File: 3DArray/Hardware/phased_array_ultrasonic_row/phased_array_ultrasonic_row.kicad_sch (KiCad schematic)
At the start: 16 parts, among them J1 Conn_02x09_Counter_Clockwise, J2 Conn_02x09_Counter_Clockwise, U1 SN74HC157, U2 SN74HC157

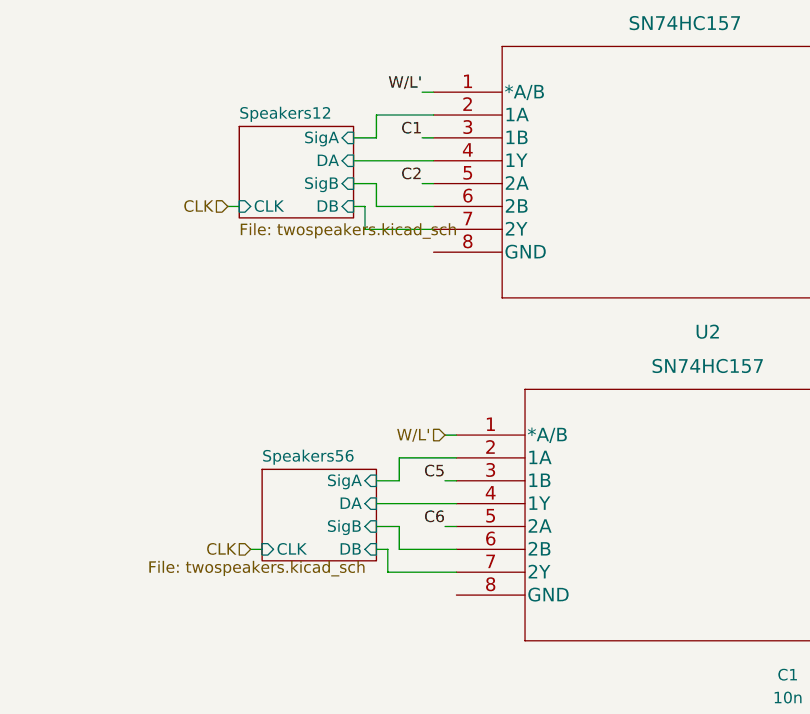
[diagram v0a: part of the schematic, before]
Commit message: Fixed pcb mux inpits swapped for C6, C6.
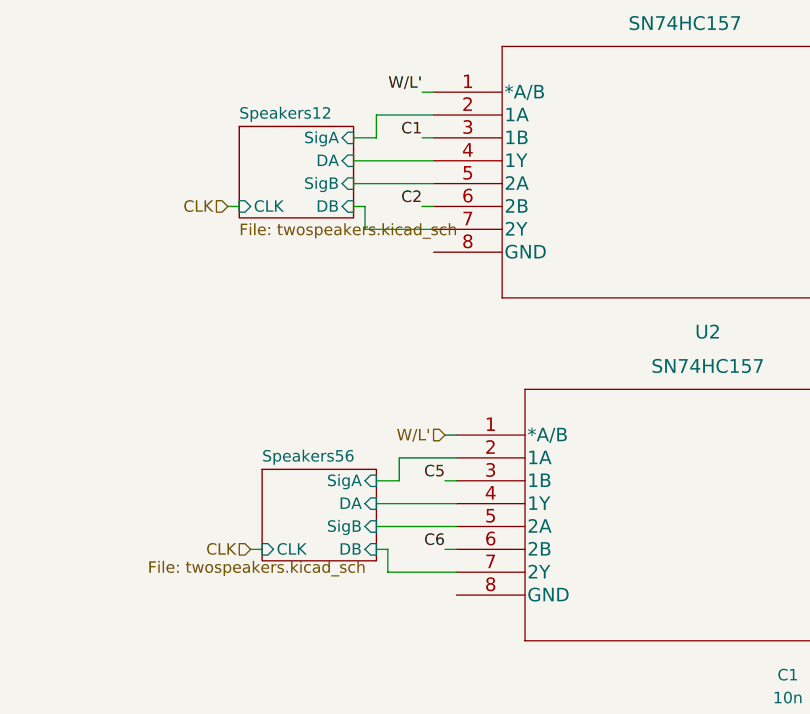
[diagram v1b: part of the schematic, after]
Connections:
- net C2: now also U1.6 (2B); no longer U1.5 (2A)
- net C6: now also U2.6 (2B); no longer U2.5 (2A)
- net Speakers12/SigB: now also U1.5 (2A); no longer U1.6 (2B)
- net Speakers56/SigB: now also U2.5 (2A); no longer U2.6 (2B)
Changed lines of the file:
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@@
     (stroke (width 0) (type default) (color 0 0 0 0))
   )
-  (wire (pts (xy 111.76 87.63) (xy 114.3 87.63))
-    (stroke (width 0) (type default) (color 0 0 0 0))
-  )
-  (wire (pts (xy 109.22 49.53) (xy 111.76 49.53))
+  (wire (pts (xy 109.22 49.53) (xy 118.11 49.53))
     (stroke (width 0) (type default) (color 0 0 0 0))
   )
@@
     (stroke (width 0) (type default) (color 0 0 0 0))
   )
+  (wire (pts (xy 116.84 52.07) (xy 118.11 52.07))
+    (stroke (width 0) (type default) (color 0 0 0 0))
+  )
   (wire (pts (xy 25.4 102.87) (xy 27.94 102.87))
     (stroke (width 0) (type default) (color 0 0 0 0))
@@
     (stroke (width 0) (type default) (color 0 0 0 0))
   )
-  (wire (pts (xy 120.65 90.17) (xy 114.3 90.17))
-    (stroke (width 0) (type default) (color 0 0 0 0))
-  )
   (wire (pts (xy 116.84 44.45) (xy 118.11 44.45))
     (stroke (width 0) (type default) (color 0 0 0 0))
@@
     (stroke (width 0) (type default) (color 0 0 0 0))
   )
+  (wire (pts (xy 111.76 87.63) (xy 120.65 87.63))
+    (stroke (width 0) (type default) (color 0 0 0 0))
+  )
   (wire (pts (xy 25.4 69.85) (xy 27.94 69.85))
     (stroke (width 0) (type default) (color 0 0 0 0))
@@
     (stroke (width 0) (type default) (color 0 0 0 0))
   )
-  (wire (pts (xy 119.38 87.63) (xy 120.65 87.63))
-    (stroke (width 0) (type default) (color 0 0 0 0))
-  )
   (wire (pts (xy 40.64 90.17) (xy 44.45 90.17))
     (stroke (width 0) (type default) (color 0 0 0 0))
@@
     (stroke (width 0) (type default) (color 0 0 0 0))
   )
-  (wire (pts (xy 114.3 87.63) (xy 114.3 90.17))
-    (stroke (width 0) (type default) (color 0 0 0 0))
-  )
   (wire (pts (xy 114.3 80.01) (xy 114.3 82.55))
     (stroke (width 0) (type default) (color 0 0 0 0))
   )
-  (wire (pts (xy 111.76 49.53) (xy 111.76 52.07))
-    (stroke (width 0) (type default) (color 0 0 0 0))
-  )
   (wire (pts (xy 116.84 39.37) (xy 118.11 39.37))
     (stroke (width 0) (type default) (color 0 0 0 0))
   )
-  (wire (pts (xy 118.11 52.07) (xy 111.76 52.07))
-    (stroke (width 0) (type default) (color 0 0 0 0))
-  )
   (wire (pts (xy 173.99 41.91) (xy 175.26 41.91))
     (stroke (width 0) (type default) (color 0 0 0 0))
@@
     (stroke (width 0) (type default) (color 0 0 0 0))
   )
-  (wire (pts (xy 116.84 49.53) (xy 118.11 49.53))
-    (stroke (width 0) (type default) (color 0 0 0 0))
-  )
   (bus (pts (xy 53.34 133.35) (xy 53.34 139.7))
     (stroke (width 0) (type default) (color 0 0 0 0))
@@
     (stroke (width 0) (type default) (color 0 0 0 0))
   )
+  (wire (pts (xy 119.38 90.17) (xy 120.65 90.17))
+    (stroke (width 0) (type default) (color 0 0 0 0))
+  )
   (wire (pts (xy 55.88 148.59) (xy 59.69 148.59))
     (stroke (width 0) (type default) (color 0 0 0 0))
@@
     (effects (font (size 1.27 1.27)) (justify right bottom))
   )
-  (label "C6" (at 119.38 87.63 180)
+  (label "C6" (at 119.38 90.17 180)
     (effects (font (size 1.27 1.27)) (justify right bottom))
   )
@@
     (effects (font (size 1.27 1.27)) (justify left bottom))
   )
-  (label "C2" (at 116.84 49.53 180)
-    (effects (font (size 1.27 1.27)) (justify right bottom))
-  )
+  (label "C2" (at 116.84 52.07 180)
+    (effects (font (size 1.27 1.27)) (justify right bottom))
+  )
